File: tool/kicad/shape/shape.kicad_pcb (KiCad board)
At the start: 2 copper layers, 71.9 x 39.3 mm, 91 parts, among them J1 MICRO-USB-AB, K1 CONN_3, P10 TEST_POINT, P27 TEST_POINT, P28 TEST_POINT, P29 TEST_POINT, P30 CONN_3X2, P31 CONN_7, P35 CONN_6, P37 TEST_POINT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

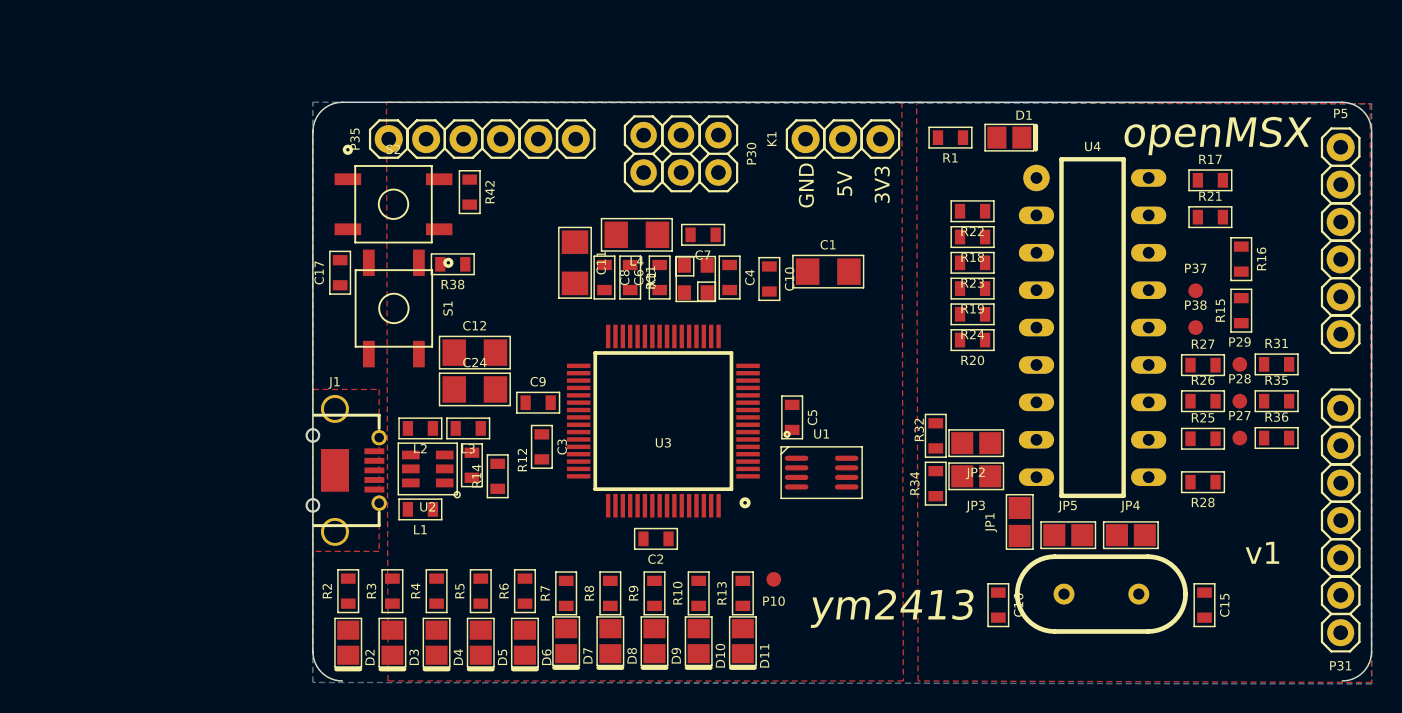
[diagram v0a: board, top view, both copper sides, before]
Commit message: shape board schematic
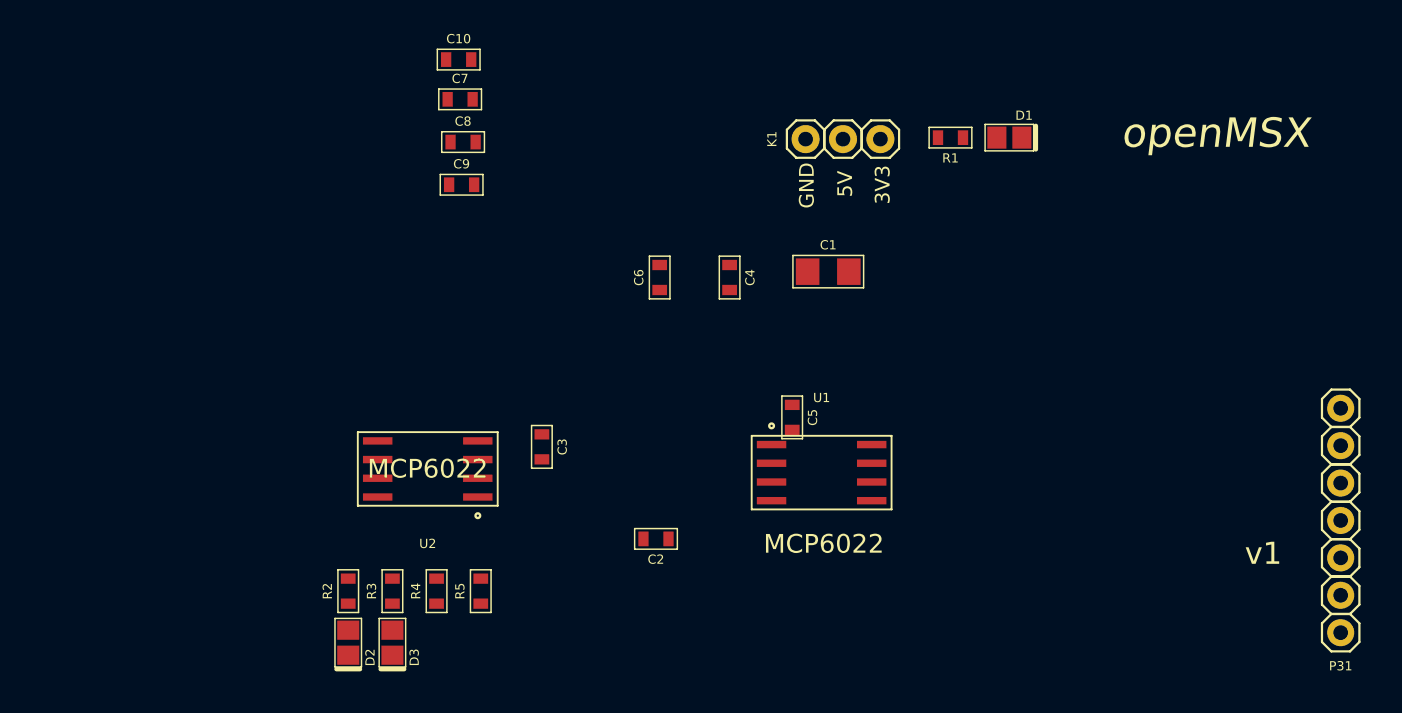
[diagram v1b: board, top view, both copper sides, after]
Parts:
- removed C11: 10uF, pretty:1206
- removed C12, C24: 4.7uF, pretty:1206
- removed C15, C16: 20pF/NC, pretty:0603_S
- removed C17: 100nF, pretty:0603_S
- removed D10, D11, D4, D5, D6, D7, D8, D9: LED, pretty:0805_LED
- removed J1: MICRO-USB-AB, pretty:USB-MICRO-AB-Molex-47590-0001
- removed JP1, JP2, JP3, JP4, JP5: SJ, pretty:Solder_Jumper_1.5mm
- removed L1, L2, L3: FB, pretty:0603_S
- removed L4: L, pretty:1206
- removed P10, P27, P28, P29, P37, P38: TEST_POINT, pretty:Test_Pad_1mm
- removed P30: CONN_3X2, pretty:PIN_2X3_ALT_S
- removed P35, P5: CONN_6, pretty:PIN_1X6_S
- removed R10, R13, R6, R7, R8, R9: 3k3, pretty:0603_S_R
- removed R11: 1, pretty:0603_S_R
- removed R12, R14: 15, pretty:0603_S_R
- removed R15, R16: 2k2, pretty:0603_S_R
- removed R17, R18, R19, R20, R21, R22, R23, R24, R25, R26, R27, R28, R32, R34: 22, pretty:0603_S_R
- removed R31, R35: 100k, pretty:0603_S_R
- removed R36: 100k/NC, pretty:0603_S_R
- removed R38, R42: 100, pretty:0603_S_R
- removed S1, S2: TACTSW, pretty:BUTTON_ALPS_SMD_5.2mm_SKQG_S
- removed U3: EFM32GG332, pretty:TQFP64
- removed U4: YM2413, pretty:DIL18
- removed X1: 48Mhz, pretty:CRYSTAL-TXC-8Z-2.5x2
- removed X2: CRYSTAL, HC-49V
- C1: value 10uF -> 0.1uF
- C10, C8: value 10nF -> 1nF
- C2, C3: value 100nF -> 0.1uF
- C4: value 18pF -> 0.1uF
- C5: value 100nF -> 1uF
- C6: value 18pF -> 1uF
- D2, D3: value LED -> D
- R2, R3, R4, R5: value 3k3 -> R
- U1: value SN74LVC2T45 -> MCP6022; footprint pretty:R-PDSO-G8 -> pretty:ATMEL_SO8
- U2: value ST-USBLC6-2 -> MCP6022; footprint pretty:SOT-23-6L -> pretty:ATMEL_SO8
- moved C10 25.8 mm to (94.1, 70.7), turned to 0 degrees
- moved C7 18.9 mm to (94.2, 73.4), turned to 0 degrees
- moved C9 15.7 mm to (94.3, 79.2)
- moved C8 13.3 mm to (94.4, 76.3), turned to 0 degrees
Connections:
- C1 pad 1: GND -> /MO
- C1 pad 2: +3.3V -> Net-(C1-Pad2)
- C10 pad 2: +3.3VADC -> +3.3V
- C2 pad 1: GND -> /RO
- C2 pad 2: +3.3V -> Net-(C2-Pad2)
- C3 pad 2: +3.3V -> +5V
- C4 pad 2: /XTP -> +5V
- C5 pad 2: +3.3V -> +5V
- C6 pad 2: /XTN -> +5V
- C7 pad 2: +3.3V -> +5V
- C8 pad 2: +3.3VADC -> +5V
- C9 pad 2: /DECOUPLE -> +3.3V
- D2 pad 2: GND -> Net-(C1-Pad2)
- D3 pad 2: GND -> Net-(C2-Pad2)
- P31 pad 3: +5V -> Net-(P31-Pad3)
- R2 pad 1: Net-(D2-Pad1) -> Net-(R2-Pad1)
- R2 pad 2: /LED0 -> GND
- R3 pad 1: Net-(D3-Pad1) -> Net-(R3-Pad1)
- R3 pad 2: /LED1 -> GND
- R4 pad 1: Net-(D4-Pad1) -> /MO_SAMPLE
- R4 pad 2: /LED2 -> Net-(R2-Pad1)
- R5 pad 1: Net-(D5-Pad1) -> /RO_SAMPLE
- R5 pad 2: /LED3 -> Net-(R3-Pad1)
- U1 pad 1: +3.3V -> Net-(D2-Pad1)
- U1 pad 2: /XIN3V3 -> Net-(C1-Pad2)
- U1 pad 3: /XOUT3V3 -> GND
- U1 pad 5: +3.3V -> Net-(D2-Pad1)
- U1 pad 6: /XOUT -> Net-(R2-Pad1)
- U1 pad 7: /XIN -> /MO_SAMPLE
- U2 pad 1: /D-B -> Net-(D3-Pad1)
- U2 pad 2: GND -> Net-(C2-Pad2)
- U2 pad 3: /D+B -> GND
- U2 pad 4: /D+_IN -> GND
- U2 pad 5: /VBUS_IN -> Net-(D3-Pad1)
- U2 pad 6: /D-_IN -> Net-(R3-Pad1)
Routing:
- removed copper zone on F.Cu, net +3.3V
- removed copper zone on F.Cu, net +5V
- removed copper zone on F.Cu, net /GI_2
- removed copper zone on B.Cu, net GND
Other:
- board outline removed
- board text removed: "ym2413"

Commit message: rough layout
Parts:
- C1: footprint pretty:1206 -> pretty:0603_S
- moved P31 84.0 mm to (70.0, 100.0)
- moved C1 48.2 mm to (73.4, 100.0)
- moved D1 44.0 mm to (98.6, 105.2), turned to 270 degrees
- moved C10 40.9 mm to (74.4, 106.6), turned to 90 degrees
- moved R1 38.2 mm to (98.6, 101.0), turned to 90 degrees
- moved C7 36.3 mm to (72.6, 102.6), turned to 90 degrees
- moved U1 35.0 mm to (84.2, 104.2)
- moved C9 35.0 mm to (72.6, 106.6), turned to 90 degrees
- moved C2 34.6 mm to (73.4, 97.4), turned to 0 degrees
- moved C8 33.0 mm to (74.4, 102.6), turned to 90 degrees
- moved K1 28.0 mm to (98.8, 94.2), turned to 0 degrees
- moved C5 27.5 mm to (90.0, 101.4), turned to 90 degrees
- moved C4 23.7 mm to (90.0, 93.0), turned to 90 degrees
- moved C6 21.4 mm to (87.4, 92.2), turned to 0 degrees
- moved D3 20.2 mm to (78.0, 93.8)
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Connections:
- net Net-(C1-Pad2) renamed /MOA
- net Net-(C2-Pad2) renamed /ROA
- net Net-(D2-Pad1) renamed /MOO
- net Net-(D3-Pad1) renamed /ROO
- P31 pad 3: Net-(P31-Pad3) -> +5V

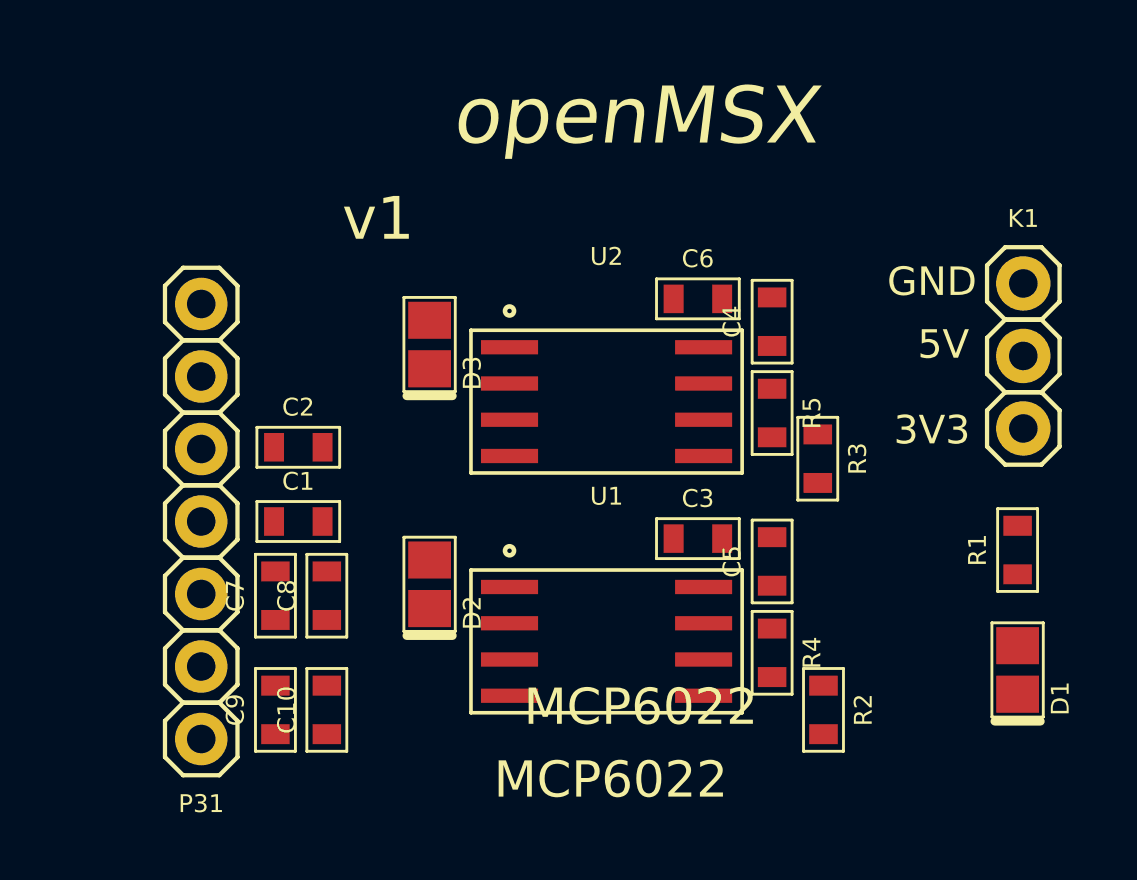
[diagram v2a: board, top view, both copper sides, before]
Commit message: finish shape pcb
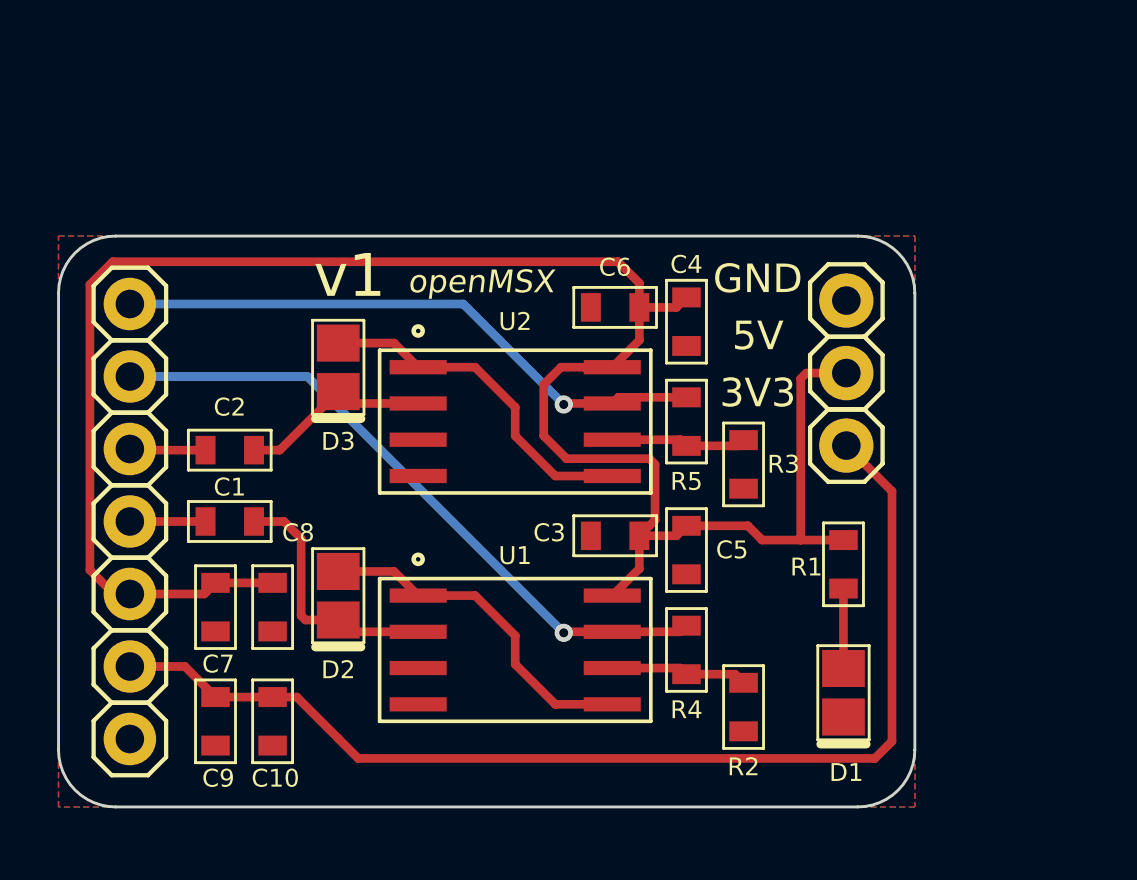
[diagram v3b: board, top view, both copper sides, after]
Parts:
- moved K1 6.23 mm to (92.6, 94.8)
- moved D1 6.15 mm to (92.5, 106.0)
- moved R1 6.12 mm to (92.5, 101.5)
- moved D3 3.30 mm to (74.8, 94.6)
- moved U2 3.28 mm to (81.0, 96.5)
- moved D2 3.22 mm to (74.8, 102.6)
- moved U1 3.21 mm to (81.0, 104.5)
- moved C5 3.03 mm to (87.0, 101.0)
- moved R5 3.01 mm to (87.0, 96.5)
- moved R4 3.00 mm to (87.0, 104.5)
- moved C4 3.00 mm to (87.0, 93.0)
- moved C6 2.92 mm to (84.5, 92.5)
- moved C3 2.90 mm to (84.5, 100.5)
- moved R2 2.80 mm to (89.0, 106.5)
- moved R3 2.61 mm to (89.0, 98.0)
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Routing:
- net +5V: track 0.00 -> 71.8 mm
- net +3.3V: track 0.00 -> 39.3 mm
- net /MO_SAMPLE: track 0.00 -> 23.3 mm, vias 0 -> 1
- net /RO_SAMPLE: track 0.00 -> 21.1 mm, vias 0 -> 1
- net /ROO: track 0.00 -> 12.1 mm
- net /MOO: track 0.00 -> 12.1 mm
- net /MOA: track 0.00 -> 8.93 mm
- net /ROA: track 0.00 -> 6.77 mm
- net Net-(R2-Pad1): track 0.00 -> 4.81 mm
- net Net-(R3-Pad1): track 0.00 -> 4.77 mm
- net Net-(D1-Pad1): track 0.00 -> 2.80 mm
- net /RO: track 0.00 -> 2.67 mm
- net /MO: track 0.00 -> 2.65 mm
- added copper zone on B.Cu, net GND
- added copper zone on F.Cu, net GND
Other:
- board outline added: 30 x 20 mm
- net class Default: trace_width 0.2032 -> 0.3048
- board text added: "MO"
- board text added: "MOS"
- board text added: "RO"
- board text added: "ROS"

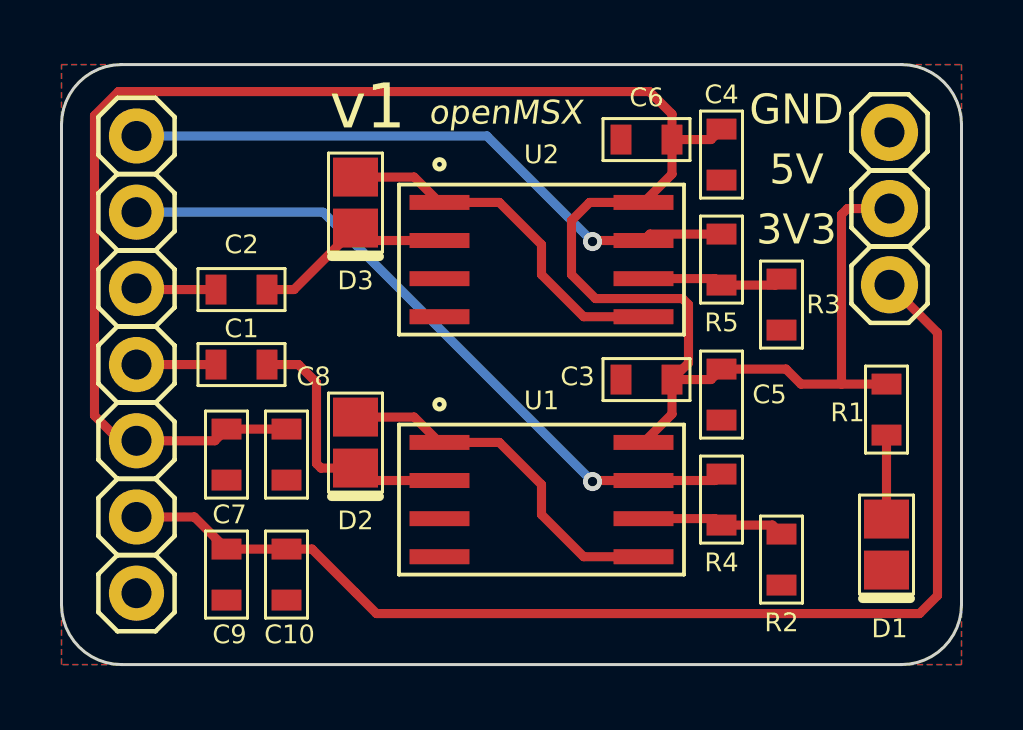
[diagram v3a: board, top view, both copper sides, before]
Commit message: updated shaper board design (tested in breadboard)
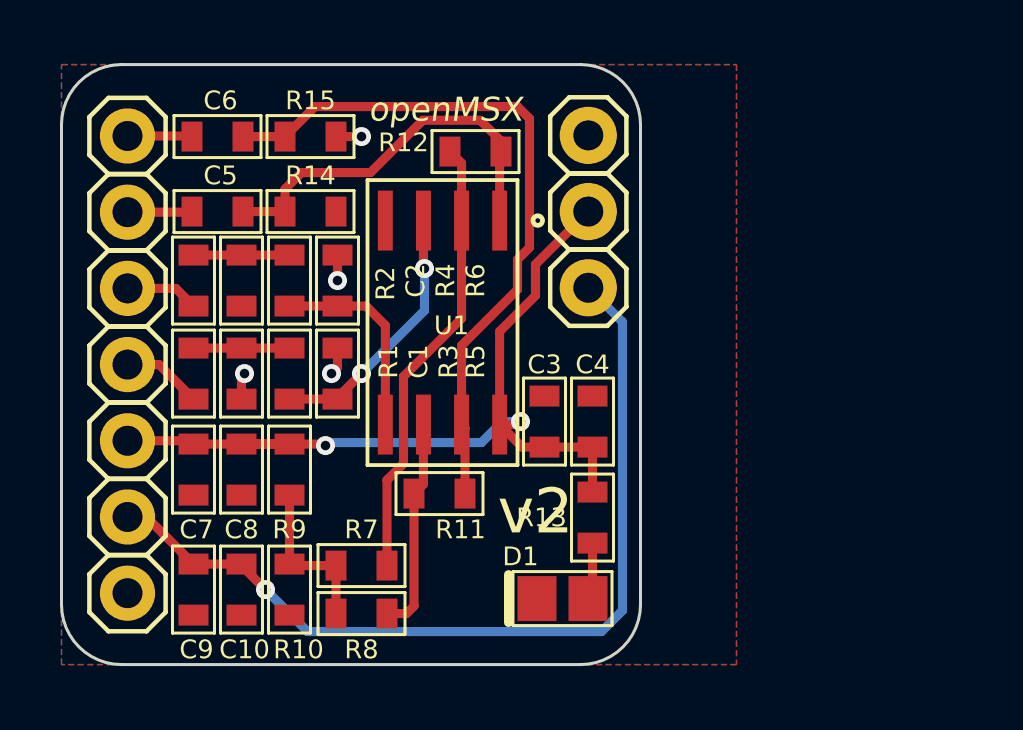
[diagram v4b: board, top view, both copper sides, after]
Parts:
- removed D2, D3: D, pretty:0805_LED
- removed P31: CONN_7, pretty:PIN_1X7_S
- removed U2: MCP6022, pretty:ATMEL_SO8
- added P1: CONN_7, pretty:PIN_1X7_S, F.Cu at (67.2, 100.0)
- added R10: 1.5k, pretty:0603_S_R, F.Cu at (72.6, 107.5)
- added R11: 100k, pretty:0603_S_R, F.Cu at (77.6, 104.3)
- added R12: 100k, pretty:0603_S_R, F.Cu at (78.8, 92.9)
- added R13: 3k3, pretty:0603_S_R, F.Cu at (82.7, 105.1)
- added R14: 100, pretty:0603_S_R, F.Cu at (73.3, 94.9)
- added R15: 100, pretty:0603_S_R, F.Cu at (73.3, 92.4)
- added R6: 100k, pretty:0603_S_R, F.Cu at (74.2, 97.2)
- added R7: 22k, pretty:0603_S_R, F.Cu at (75.0, 106.7)
- added R8: 22k, pretty:0603_S_R, F.Cu at (75.0, 108.3)
- added R9: 1k, pretty:0603_S_R, F.Cu at (72.6, 103.5)
- C1, C2: value 0.1uF -> 2.2nF
- C4: value 0.1uF -> 1uF
- C5, C6: value 1uF -> 0.1uF
- R1: value 3k3 -> 2.2k
- R2: value R -> 2.2k
- R3, R4: value R -> 22k
- R5: value R -> 100k
- moved R1 23.1 mm to (69.4, 100.3)
- moved R2 21.7 mm to (69.4, 97.2), turned to 90 degrees
- moved C5 17.9 mm to (70.2, 94.9), turned to 180 degrees
- moved R3 16.6 mm to (72.6, 100.3)
- moved R4 16.1 mm to (72.6, 97.2)
- moved C6 14.3 mm to (70.2, 92.4), turned to 180 degrees
- moved R5 13.4 mm to (74.2, 100.3), turned to 90 degrees
- moved D1 10.9 mm to (81.7, 107.8), turned to 180 degrees
- moved K1 10.0 mm to (82.6, 94.9)
- moved C4 9.88 mm to (82.7, 101.9), turned to 270 degrees
- moved U1 6.76 mm to (77.7, 98.6), turned to 270 degrees
- moved C3 3.68 mm to (81.1, 101.9), turned to 270 degrees
- moved C10 1.58 mm to (71.0, 107.5)
- moved C8 1.58 mm to (71.0, 103.5)
- moved C7 1.21 mm to (69.4, 103.5)
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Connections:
- C1 pad 1: /MO -> /MOA
- C1 pad 2: /MOA -> GND
- C2 pad 1: /RO -> /ROA
- C2 pad 2: /ROA -> GND
- C5 pad 1: GND -> /MOO
- C5 pad 2: +5V -> /MO_SAMPLE
- C6 pad 1: GND -> /ROO
- C6 pad 2: +5V -> /RO_SAMPLE
- R1 pad 1: Net-(D1-Pad1) -> /MO
- R1 pad 2: +5V -> /MOA
- R2 pad 1: Net-(R2-Pad1) -> /RO
- R2 pad 2: GND -> /ROA
- R3 pad 1: Net-(R3-Pad1) -> /MOA
- R3 pad 2: GND -> /MOB
- R4 pad 1: /MO_SAMPLE -> /ROA
- R4 pad 2: Net-(R2-Pad1) -> /ROB
- R5 pad 1: /RO_SAMPLE -> /MOB
- R5 pad 2: Net-(R3-Pad1) -> GND
- U1 pad 2: /MOA -> Net-(R12-Pad2)
- U1 pad 3: GND -> /MOB
- U1 pad 5: /MOO -> /ROB
- U1 pad 6: Net-(R2-Pad1) -> Net-(R11-Pad2)
- U1 pad 7: /MO_SAMPLE -> /ROO
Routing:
- net +5V: track 71.8 -> 29.1 mm, vias 0 -> 2
- net /MO_SAMPLE: track 23.3 -> 2.16 mm, vias 1 -> 0
- net /RO_SAMPLE: track 21.1 -> 2.16 mm, vias 1 -> 0
- net Net-(R12-Pad2): track 0.00 -> 15.0 mm
- net /ROO: track 12.1 -> 23.6 mm
- net +3.3V: track 39.3 -> 29.6 mm, vias 0 -> 1
- net /MOB: track 0.00 -> 8.77 mm, vias 0 -> 2
- net Net-(R11-Pad2): track 0.00 -> 7.18 mm
- net /ROB: track 0.00 -> 6.77 mm
- net /MOA: track 8.93 -> 3.20 mm
- net /VREF: track 0.00 -> 5.47 mm
- net Net-(R2-Pad1): track 4.81 -> 0.00 mm
- net Net-(R3-Pad1): track 4.77 -> 0.00 mm
- net /ROA: track 6.77 -> 3.20 mm
- net GND: track 0.00 -> 3.52 mm, vias 0 -> 4
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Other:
- board size 30 x 20 mm -> 19.3 x 20 mm
- board text added: "v2"
- board text removed: "v1"

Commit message: tune shape board
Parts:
- C5, C6: value 0.1uF -> 0Ohm
- R1, R2: value 2.2k -> 0/2.2k
- R10: value 1.5k -> 1.21k
- R14, R15: value 100 -> NC
- R3, R4, R7, R8: value 22k -> 68k
- R9: value 1k -> 1.5k
- moved R15 0.11 mm to (73.2, 92.5), turned to 0 degrees
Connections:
- R15 pad 1: GND -> /ROO
- R15 pad 2: /ROO -> GND
